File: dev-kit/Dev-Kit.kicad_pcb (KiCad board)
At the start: 4 copper layers, 110 x 70 mm, 118 parts, among them IC101 nPM1300-QEXX, IC201 APDS-9306-065, IC202 RV-8263-C8, IC203 BMI270, IC204 LIS2MDLTR, IC205 BMP581, IC206 DRV2603RUNT, IC301 FAN5622SX, IC302 MX25U51245GZ4I00, IC303 USBLC6-2P6, IC304 NTS0104GU12, M301 NORA-B106, Q201 DMG1013UW-7, Q202 PMZ550UNEYL, Q203 PMZ550UNEYL, X101 Battery, X102 Battery, X103 Power, X201 Power, X202 I2S, X203 Power, X204 I2C, X205 Power, X206 Power, X207 Power, X208 Power, X209 Power, X210 Motor, X301 Power, X302 Power, X303 Device, X304 GPIO, X305 UART, X306 IO Power, X307 Display, X308 Touch Power, X309 LED Power, X310 DEBUG

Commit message: Issue #117
Signed-off-by: Daniel Kampert <DanielKampert@kampis-elektroecke.de>
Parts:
- IC301: value FAN5622SX -> FAN5624UMPX
- X201, X203, X205, X206, X207, X208, X209, X301, X302, X306, X308, X309: footprint Connector_PinHeader_2.54mm:PinHeader_1x02_P2.54mm_Vertical_SMD_Pin1Left -> Connector_PinHeader_2.54mm:PinHeader_1x02_P2.54mm_Vertical_SMD_Pin1Right
- X202: footprint Connector_PinHeader_2.54mm:PinHeader_1x05_P2.54mm_Vertical_SMD_Pin1Left -> Connector_PinHeader_2.54mm:PinHeader_1x05_P2.54mm_Vertical_SMD_Pin1Right
- X204: footprint Connector_PinHeader_2.54mm:PinHeader_1x04_P2.54mm_Vertical_SMD_Pin1Left -> Connector_PinHeader_2.54mm:PinHeader_1x04_P2.54mm_Vertical_SMD_Pin1Right
- X304: footprint Connector_PinHeader_2.54mm:PinHeader_1x06_P2.54mm_Vertical_SMD_Pin1Left -> Connector_PinHeader_2.54mm:PinHeader_1x06_P2.54mm_Vertical_SMD_Pin1Right
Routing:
- net /MCU/Data: track 89.7 -> 94.7 mm
- net Net-(X307-CTP-VDD): track 55.7 -> 51.9 mm
- net /MCU/SCL: track 134.3 -> 130.9 mm
- net Net-(IC204-VDD): track 3.17 -> 6.48 mm
- net Net-(X306-Pin_2): track 51.5 -> 54.8 mm
- net Net-(M301C-P1.14): track 40.9 -> 44.2 mm
- net Net-(M301B-P0.05/AIN1): track 32.6 -> 35.9 mm
- net Net-(M301B-P0.04/AIN0): track 38.1 -> 34.8 mm
- net Net-(M301A-VDDH): track 7.98 -> 11.3 mm
- net Net-(IC302-VCC): track 6.96 -> 10.3 mm
- net Net-(IC206-VDD): track 11.7 -> 8.41 mm
- net Net-(IC203-VDD): track 3.48 -> 6.79 mm
- net Net-(IC202-VDD): track 7.48 -> 10.8 mm
- net /Peripherals/VSYS: track 137.1 -> 140.4 mm
- net /MCU/SDA: track 146.1 -> 149.4 mm
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
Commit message: Feature: Issue #153
Signed-off-by: Daniel Kampert <DanielKampert@kampis-elektroecke.de>
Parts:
- X310: footprint Connector_PinHeader_1.27mm:PinHeader_2x05_P1.27mm_Vertical -> Samtec:SHF-105-01-L-D-SM-TR
- moved X310 1.69 mm to (210.8, 125.7)
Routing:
- net GND: track 77.4 -> 80.3 mm, vias 59 -> 60
- net SWDCLK: track 27.0 -> 28.9 mm, vias 1 -> 2
- net RESETn: track 31.1 -> 32.6 mm, vias 2 -> 3
- net SWDIO: track 26.4 -> 25.5 mm, vias 1 -> 2
- net /MCU/SCL: track 130.9 -> 130.3 mm

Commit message: Task: Issue #115
Signed-off-by: Daniel Kampert <DanielKampert@kampis-elektroecke.de>
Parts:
- removed the REF** at (109.0, 81.0)
- removed the REF** at (109.0, 143.0)
- removed the REF** at (211.0, 143.0)
- removed the REF** at (190.7, 99.5)
- moved X308 21.9 mm to (163.9, 113.0), turned to 0 degrees
- moved X309 15.6 mm to (168.0, 120.5), turned to 90 degrees
- moved REF** 10.0 mm to (162.0, 120.0)
- moved REF** 10.0 mm to (120.0, 120.0)
- moved REF** 10.0 mm to (162.0, 91.0)
- moved REF** 10.0 mm to (120.0, 91.0)
- moved X307 10.00 mm to (128.7, 105.1)
- moved X306 5.73 mm to (167.2, 97.2)
- moved S203 5.00 mm to (123.0, 129.0)
- moved S204 5.00 mm to (123.0, 83.0)
- moved kibuzzard-68304292 5.00 mm to (130.7, 82.9)
- moved kibuzzard-68304278 5.00 mm to (130.7, 128.6)
- moved X103 1.70 mm to (118.6, 135.2)
- moved G*** 1.12 mm to (173.0, 101.2)
- moved kibuzzard-68304463 1.12 mm to (175.8, 96.8)
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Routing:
- net +3V0: track 72.7 -> 51.9 mm, vias 7 -> 6
- net Net-(X306-Pin_2): track 54.8 -> 42.4 mm
- net DISPLAY-CLK: track 90.7 -> 80.7 mm
- net LEDK2: track 43.5 -> 33.5 mm
- net DISPLAY-DC: track 87.9 -> 77.9 mm
- net DISPLAY-DATA: track 90.3 -> 80.3 mm
- net DISPLAY-CS: track 87.6 -> 77.6 mm
- net Net-(IC304-B3): track 44.2 -> 34.2 mm
- net LEDK1: track 42.1 -> 32.1 mm
- net Net-(IC304-B4): track 44.3 -> 34.3 mm
- net Net-(IC304-B2): track 44.2 -> 34.2 mm
- net DISPLAY-RST: track 86.6 -> 76.6 mm
- net Net-(IC304-B1): track 44.3 -> 34.3 mm
- net Net-(X307-LEDA1): track 40.5 -> 48.5 mm
- net /MCU/SW4: track 154.8 -> 149.5 mm, vias 2 -> 4
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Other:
- board size 110 x 70 mm -> 100 x 70 mm

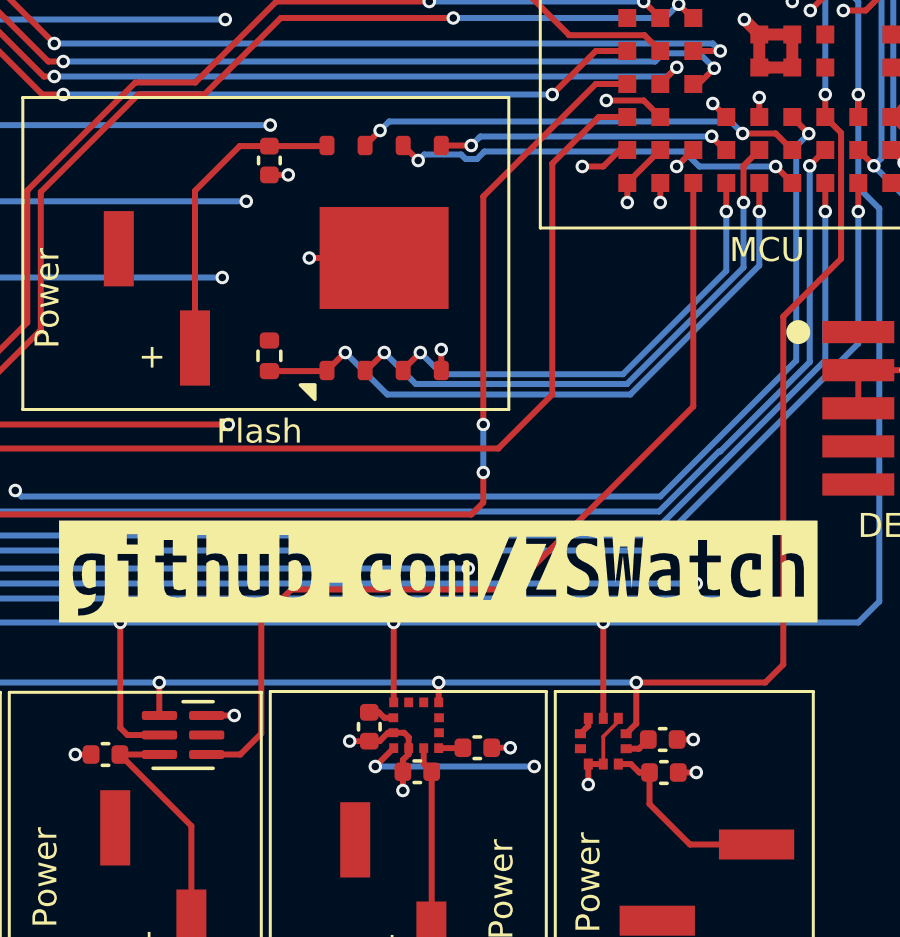
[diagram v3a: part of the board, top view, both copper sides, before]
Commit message: Task: Issue #122
Signed-off-by: Daniel Kampert <DanielKampert@kampis-elektroecke.de>
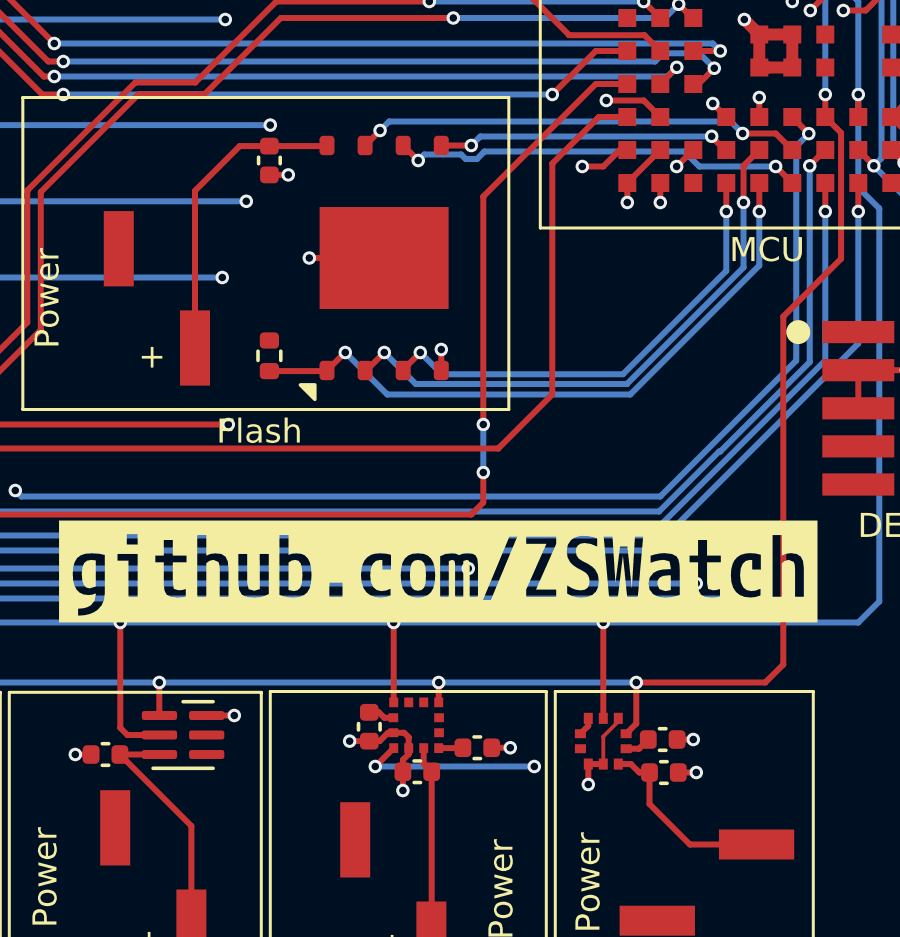
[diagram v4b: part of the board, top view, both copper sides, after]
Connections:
- IC201 pad 4: /MCU/APDS-INT -> unconnected-(IC201-INT-Pad4)
- M301 pad C1: /MCU/APDS-INT -> unconnected-(M301B-P0.10/TRACEDATA[1]-PadC1)
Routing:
- net /MCU/APDS-INT: track 30.7 -> 0.00 mm
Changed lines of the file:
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@@
 	(net 18 "TOUCH-RST")
 	(net 19 "DISPLAY-EN")
-	(net 20 "/MCU/APDS-INT")
+	(net 20 "unconnected-(IC201-INT-Pad4)")
 	(net 21 "Net-(MK201-VDD)")
 	(net 22 "Net-(IC204-C1)")
@@
 	(net 145 "unconnected-(X310-NC{slash}TDI-Pad8)")
 	(net 146 "unconnected-(X310-KEY-Pad7)")
+	(net 147 "unconnected-(M301B-P0.10{slash}TRACEDATA[1]-PadC1)")
 	(footprint "Resistor_SMD:R_0805_2012Metric"
 		(layer "F.Cu")
@@
 			)
 		)
-		(property "Datasheet" ""
+		(property "Datasheet" "~"
 			(at 0 0 0)
 			(unlocked yes)
@@
 			(layers "F.Cu" "F.Mask" "F.Paste")
 			(roundrect_rratio 0.25)
-			(net 20 "/MCU/APDS-INT")
+			(net 20 "unconnected-(IC201-INT-Pad4)")
 			(pinfunction "INT")
-			(pintype "open_collector")
+			(pintype "open_collector+no_connect")
 		)
 		(pad "5" smd roundrect
@@
 			)
 		)
-		(property "Datasheet" ""
+		(property "Datasheet" "~"
 			(at 0 0 0)
 			(unlocked yes)
@@
 			)
 		)
-		(property "Datasheet" ""
+		(property "Datasheet" "~"
 			(at 0 0 0)
 			(unlocked yes)
@@
 			)
 		)
-		(property "Datasheet" ""
+		(property "Datasheet" "~"
 			(at 0 0 0)
 			(unlocked yes)
@@
 			)
 		)
-		(property "Datasheet" ""
+		(property "Datasheet" "~"
 			(at 0 0 0)
 			(unlocked yes)
@@
 			(size 0.6 0.6)
 			(layers "F.Cu" "F.Mask" "F.Paste")
-			(net 20 "/MCU/APDS-INT")
+			(net 147 "unconnected-(M301B-P0.10{slash}TRACEDATA[1]-PadC1)")
 			(pinfunction "P0.10/TRACEDATA[1]")
-			(pintype "bidirectional")
+			(pintype "bidirectional+no_connect")
 		)
 		(pad "C2" smd rect
@@
 			)
 		)
-		(property "Datasheet" ""
+		(property "Datasheet" "~"
 			(at 0 0 0)
 			(unlocked yes)
@@
 			)
 		)
-		(property "Datasheet" ""
+		(property "Datasheet" "~"
 			(at 0 0 0)
 			(unlocked yes)
@@
 			)
 		)
-		(property "Datasheet" ""
+		(property "Datasheet" "~"
 			(at 0 0 0)
 			(unlocked yes)
@@
 	)
 	(segment
-		(start 187.08 137.2)
-		(end 188.2 137.2)
-		(width 0.2)
-		(layer "F.Cu")
-		(net 20)
-	)
-	(segment
-		(start 189.9 131.7)
-		(end 197.2 131.7)
-		(width 0.2)
-		(layer "F.Cu")
-		(net 20)
-	)
-	(segment
-		(start 203.3 125.6)
-		(end 203.3 118.15)
-		(width 0.2)
-		(layer "F.Cu")
-		(net 20)
-	)
-	(segment
-		(start 188.9 132.7)
-		(end 189.9 131.7)
-		(width 0.2)
-		(layer "F.Cu")
-		(net 20)
-	)
-	(segment
-		(start 197.2 131.7)
-		(end 203.3 125.6)
-		(width 0.2)
-		(layer "F.Cu")
-		(net 20)
-	)
-	(segment
-		(start 188.2 137.2)
-		(end 188.9 136.5)
-		(width 0.2)
-		(layer "F.Cu")
-		(net 20)
-	)
-	(segment
-		(start 188.9 136.5)
-		(end 188.9 132.7)
-		(width 0.2)
-		(layer "F.Cu")
-		(net 20)
-	)
-	(segment

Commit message: Bug: Issue #121
Signed-off-by: Daniel Kampert <DanielKampert@kampis-elektroecke.de>
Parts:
- X201, X203, X205, X206, X207, X208, X209, X301, X302, X306, X308, X309: footprint Connector_PinHeader_2.54mm:PinHeader_1x02_P2.54mm_Vertical_SMD_Pin1Right -> Connector_PinHeader_2.54mm:PinHeader_1x02_P2.54mm_Vertical
- X202: footprint Connector_PinHeader_2.54mm:PinHeader_1x05_P2.54mm_Vertical_SMD_Pin1Right -> Connector_PinHeader_2.54mm:PinHeader_1x05_P2.54mm_Vertical
- X204: footprint Connector_PinHeader_2.54mm:PinHeader_1x04_P2.54mm_Vertical_SMD_Pin1Right -> Connector_PinHeader_2.54mm:PinHeader_1x04_P2.54mm_Vertical
- X304: footprint Connector_PinHeader_2.54mm:PinHeader_1x06_P2.54mm_Vertical_SMD_Pin1Right -> Connector_PinHeader_2.54mm:PinHeader_1x06_P2.54mm_Vertical
- moved kibuzzard-68304463 12.1 mm to (186.5, 102.4), turned to 0 degrees
- moved G*** 9.25 mm to (182.1, 99.6), turned to 0 degrees
- moved X304 7.99 mm to (175.5, 112.0)
- moved X202 5.13 mm to (138.5, 133.0)
- moved X204 3.70 mm to (151.8, 135.5)
- moved X302 2.80 mm to (182.7, 122.6), turned to 180 degrees
- moved X101 2.54 mm to (178.9, 79.5), turned to -90 degrees
- moved X308 2.50 mm to (166.0, 111.7), turned to -90 degrees
- moved X306 2.46 mm to (169.4, 96.1)
- moved X203 2.08 mm to (132.1, 138.4), turned to 0 degrees
- moved X207 1.74 mm to (194.8, 142.5), turned to -90 degrees
- moved X103 1.60 mm to (120.2, 135.2)
- moved X205 1.54 mm to (160.2, 140.3)
- moved X201 1.50 mm to (186.2, 142.5), turned to -90 degrees
- moved C205 1.33 mm to (177.7, 138.3)
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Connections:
- X101 pad 1: GND -> /Peripherals/VBAT
- X101 pad 2: /Peripherals/VBAT -> GND
- X301 pad 1: Net-(M301A-VDDH) -> +1V8
- X301 pad 2: +1V8 -> Net-(M301A-VDDH)
- X302 pad 1: Net-(IC302-VCC) -> +1V8
- X302 pad 2: +1V8 -> Net-(IC302-VCC)
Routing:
- net GND: track 79.9 -> 74.5 mm, vias 60 -> 56
- net /MCU/SW4: track 149.5 -> 144.4 mm
- net /MCU/~{RTC-INT}: track 62.5 -> 57.7 mm
- net /MCU/SDA: track 149.4 -> 145.1 mm, vias 8 -> 7
- net /Peripherals/VSYS: track 142.1 -> 138.3 mm, vias 5 -> 4
- net Net-(IC202-VDD): track 11.0 -> 8.44 mm
- net /MCU/WS: track 87.4 -> 89.8 mm, vias 3 -> 2
- net +3V0: track 51.9 -> 49.7 mm, vias 6 -> 4
- net /MCU/Data: track 94.7 -> 92.7 mm, vias 3 -> 2
- net Net-(M301B-P0.04/AIN0): track 33.8 -> 35.8 mm, vias 3 -> 2
- net DISPLAY-BLK: track 46.7 -> 45.0 mm
- net Net-(IC206-VDD): track 8.41 -> 10.1 mm
- net /Peripherals/VBAT: track 23.2 -> 21.5 mm, vias 5 -> 4
- net Net-(M301A-VDDH): track 11.3 -> 9.84 mm
- net Net-(M301C-P1.14): track 43.2 -> 41.9 mm, vias 3 -> 2
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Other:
- board text added: "+1V8"
- board text added: "+3V0"
- board text added: "VSYS"

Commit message: Task: Issue #123
Signed-off-by: Daniel Kampert <DanielKampert@kampis-elektroecke.de>
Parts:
- added R315: 100k, Resistor_SMD:R_0805_2012Metric, F.Cu at (169.5, 107.6)
- added R316: 100k, Resistor_SMD:R_0805_2012Metric, F.Cu at (167.5, 107.6)
- moved X306 3.79 mm to (166.6, 93.5), turned to 0 degrees
- moved X309 0.80 mm to (169.0, 119.6)
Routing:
- net DISPLAY-EN: track 50.0 -> 53.3 mm
- net GND: track 74.5 -> 75.4 mm, vias 56 -> 57
- net Net-(X307-LEDA1): track 47.5 -> 48.3 mm
